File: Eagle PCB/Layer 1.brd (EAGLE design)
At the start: 196 x 185.3 mm, 247 parts, among them M1C1 33nF, M1C2 680uF, M1C3 1.0uF, M1D1 RED, M1D2 BLUE, M1J1 XT30PB-F, M1Q1 AOD482, M1R1 1k, M1R10 1k, M1R11 10k, M1R12 4.7k, M1R2 1k, M1R3 3.3k, M1R4 3.3k, M1R5 1k, M1R6 1k, M1R7 1k, M1R8 10k, M1R9 10k, M2C1 33nF, M2C2 680uF, M2C3 1.0uF, M2D1 RED, M2D2 BLUE, M2J1 XT30PB-F, M2Q1 AOD482, M2R1 1k, M2R10 1k, M2R11 10k, M2R12 4.7k, M2R2 1k, M2R3 3.3k, M2R4 3.3k, M2R5 1k, M2R6 1k, M2R7 1k, M2R8 10k, M2R9 10k, M3C1 33nF, M3C2 680uF, M3C3 1.0uF, M3D1 RED, M3D2 BLUE, M3J1 XT30PB-F, M3Q1 AOD482, M3R1 1k, M3R10 1k, M3R11 10k, M3R12 4.7k, M3R2 1k, M3R3 3.3k, M3R4 3.3k, M3R5 1k, M3R6 1k, M3R7 1k, M3R8 10k, M3R9 10k, M4C1 33nF, M4C2 680uF, M4C3 1.0uF, M4D1 RED, M4D2 BLUE, M4J1 XT30PB-F, M4Q1 AOD482, M4R1 1k, M4R10 1k, M4R11 10k, M4R12 4.7k, M4R2 1k, M4R3 3.3k, M4R4 3.3k, M4R5 1k, M4R6 1k, M4R7 1k, M4R8 10k, M4R9 10k, Q37 AO3402, X2 SM06B-SRSS-TB, Y1 8MHz

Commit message: Fucking Done
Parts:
- moved ESC_OUT 50.1 mm to (34.1, -75.6)
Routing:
- net V_BATT: track 292.6 -> 340.9 mm
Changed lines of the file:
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@@
 <attribute name="VALUE" x="-20.433" y="-71.66" size="0.7112" layer="27" font="vector" ratio="18" rot="R90" align="top-center"/>
 </element>
-<element name="ESC_OUT" library="JH" library_urn="urn:adsk.eagle:library:6027132" package="XT30PB-F" package3d_urn="urn:adsk.eagle:package:15925142/7" value="XT30PB-F" x="-15.84" y="-79.46" smashed="yes" rot="R270">
-<attribute name="NAME" x="-12.665" y="-74.38" size="1.27" layer="25" rot="R270"/>
+<element name="ESC_OUT" library="JH" library_urn="urn:adsk.eagle:library:6027132" package="XT30PB-F" package3d_urn="urn:adsk.eagle:package:15925142/7" value="XT30PB-F" x="34.06" y="-75.56" smashed="yes" rot="R270">
+<attribute name="NAME" x="37.235" y="-70.48" size="1.27" layer="25" rot="R270"/>
 </element>
 <element name="R8" library="JH" library_urn="urn:adsk.eagle:library:6027132" package="R0603" package3d_urn="urn:adsk.eagle:package:15441228/3" value="4.7k" x="-37.88" y="-77.18" smashed="yes" rot="R90">
@@
 <wire x1="-24.21" y1="-78.09" x2="-24.9" y2="-77.4" width="0.254" layer="1"/>
 <contactref element="ESC_OUT" pad="+"/>
-<wire x1="-15.84" y1="-76.96" x2="-19.14" y2="-76.96" width="0.508" layer="16"/>
-<wire x1="-19.14" y1="-76.96" x2="-24.2" y2="-71.9" width="0.508" layer="16"/>
+<wire x1="34.06" y1="-73.06" x2="-23.04" y2="-73.06" width="0.508" layer="16"/>
+<wire x1="-23.04" y1="-73.06" x2="-24.2" y2="-71.9" width="0.508" layer="16"/>
 <wire x1="25.857465625" y1="-17.3669375" x2="22.633059375" y2="14.14253125" width="0" layer="19" extent="1-1"/>
 <wire x1="-32.893753125" y1="32.263096875" x2="-1.061" y2="48.689" width="0" layer="19" extent="1-16"/>

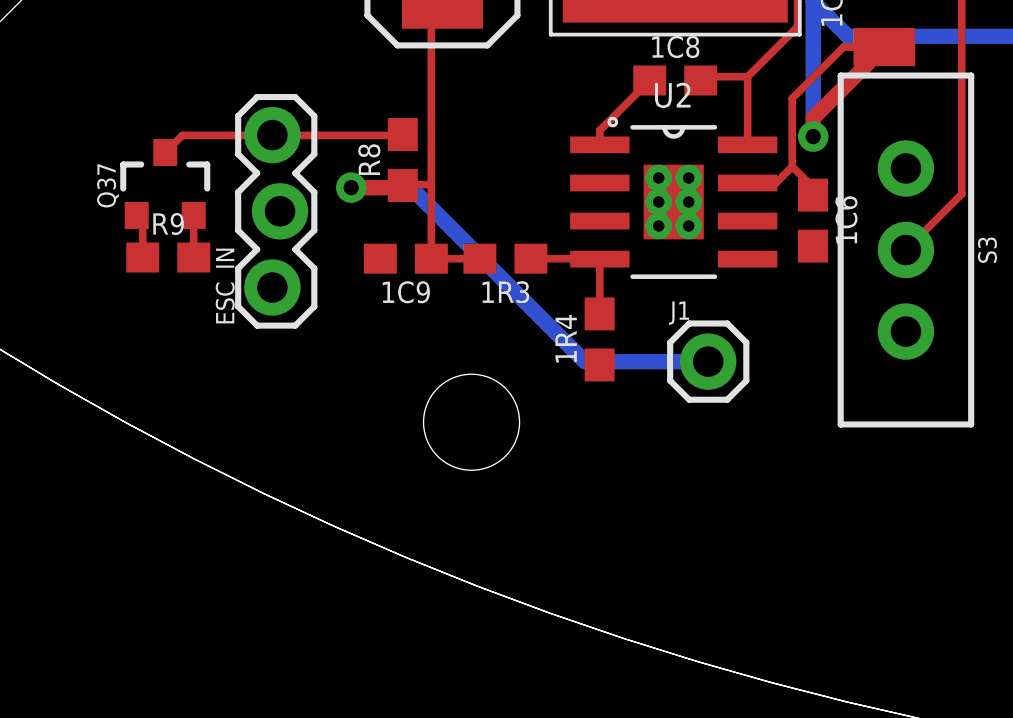
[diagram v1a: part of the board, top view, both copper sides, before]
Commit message: layer 1 esc fix
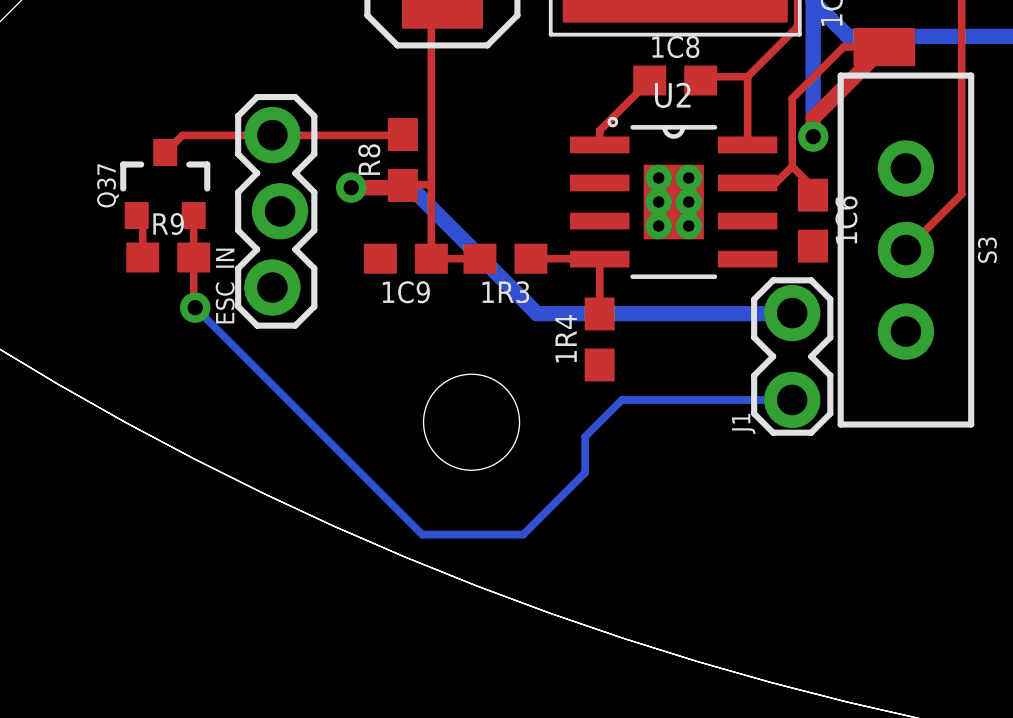
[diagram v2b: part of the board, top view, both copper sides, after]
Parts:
- J1: device Connectors:1X01 -> Connectors:1X02_LOCK
- moved J1 3.01 mm to (-24.9, -85.0), turned to 90 degrees
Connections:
- net 5V: now also J1.2; no longer J1.1
- net ESC_LV: now also J1.1
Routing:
- net ESC_LV: track 1.40 -> 28.7 mm, vias 0 -> 1
- net 5V: track 35.5 -> 37.6 mm
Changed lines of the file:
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@@
 </layers>
 <board>
-<fusionsync huburn="a.YnVzaW5lc3M6Z21haWwxNDMxNzc3" projecturn="a.YnVzaW5lc3M6Z21haWwxNDMxNzc3IzIwMjEwMTE1MzcxOTY3NzA2" f3durn="urn:adsk.wipprod:dm.lineage:Tavt4F5CTPSphMXKJUaMhw" pcbguid="" lastpulledtime="" lastsyncedchangeguid="" latestrevisionid="ff4a8119-30d6-4dfb-96ce-fc838807004c" lastsyncedrevisionid="ff4a8119-30d6-4dfb-96ce-fc838807004c" lastboardhashguid="9835a8ca-0695-94b5-924c-26b272f1dba1" lastpushedtime="2021-02-26T12:19:02Z" linktopcb3d="true"/>
+<fusionsync huburn="a.YnVzaW5lc3M6Z21haWwxNDMxNzc3" projecturn="a.YnVzaW5lc3M6Z21haWwxNDMxNzc3IzIwMjEwMTE1MzcxOTY3NzA2" f3durn="urn:adsk.wipprod:dm.lineage:Tavt4F5CTPSphMXKJUaMhw" pcbguid="" lastpulledtime="" lastsyncedchangeguid="" latestrevisionid="ff4a8119-30d6-4dfb-96ce-fc838807004c" lastsyncedrevisionid="ff4a8119-30d6-4dfb-96ce-fc838807004c" lastboardhashguid="9835a8ca-0695-94b5-924c-26b272f1dba1" lastpushedtime="2021-02-26T12:19:02Z" linktopcb3d="false"/>
 <plain>
 <circle x="88.919540625" y="-27.24548125" radius="1.6" width="0.001" layer="20"/>
@@
 <attribute name="VALUE" x="-40.068" y="-82.7" size="0.6096" layer="27" font="vector" ratio="20" rot="R90"/>
 </element>
-<element name="J1" library="Connectors" library_urn="urn:adsk.eagle:library:19813715" package="1X01" package3d_urn="urn:adsk.eagle:package:19813825/2" value="" x="-27.7" y="-83.9" smashed="yes">
-<attribute name="NAME" x="-28.97" y="-82.503" size="0.6096" layer="25" font="vector" ratio="20"/>
-<attribute name="VALUE" x="-28.97" y="-85.424" size="0.6096" layer="27" font="vector" ratio="20" align="top-left"/>
+<element name="J1" library="Connectors" library_urn="urn:adsk.eagle:library:19813715" package="1X02_LOCK" package3d_urn="urn:adsk.eagle:package:19813850/2" value="" x="-24.9" y="-85" smashed="yes" rot="R90">
+<attribute name="NAME" x="-26.297" y="-86.27" size="0.6096" layer="25" font="vector" ratio="20" rot="R90"/>
+<attribute name="VALUE" x="-22.868" y="-86.27" size="0.6096" layer="27" font="vector" ratio="20" rot="R90"/>
 </element>
 </elements>
@@
 <wire x1="-37.88" y1="-78.03" x2="-37.85" y2="-78" width="0.254" layer="1"/>
 <wire x1="-37.85" y1="-78" x2="-36.93" y2="-78" width="0.254" layer="1"/>
-<contactref element="J1" pad="1"/>
 <wire x1="-37.88" y1="-78.03" x2="-37.95" y2="-78.1" width="0.508" layer="1"/>
 <wire x1="-37.95" y1="-78.1" x2="-39.6" y2="-78.1" width="0.508" layer="1"/>
 <via x="-39.6" y="-78.1" extent="1-16" drill="0.508"/>
-<wire x1="-31.81" y1="-83.9" x2="-37.61" y2="-78.1" width="0.508" layer="16"/>
+<wire x1="-37.61" y1="-78.1" x2="-33.41" y2="-82.3" width="0.508" layer="16"/>
 <wire x1="-39.6" y1="-78.1" x2="-37.61" y2="-78.1" width="0.508" layer="16"/>
-<wire x1="-31.81" y1="-83.9" x2="-27.7" y2="-83.9" width="0.508" layer="16"/>
+<contactref element="J1" pad="2"/>
+<wire x1="-33.41" y1="-82.3" x2="-24.9178" y2="-82.3" width="0.508" layer="16"/>
+<wire x1="-24.9178" y1="-82.3" x2="-24.9" y2="-82.2822" width="0.508" layer="16"/>
 </signal>
 <signal name="ESC_HV">
@@
 <contactref element="Q37" pad="2"/>
 <wire x1="-44.85" y1="-80.43" x2="-44.85" y2="-79.03" width="0.254" layer="1"/>
+<contactref element="J1" pad="1"/>
+<wire x1="-44.85" y1="-80.43" x2="-44.85" y2="-82.05" width="0.254" layer="1"/>
+<wire x1="-44.85" y1="-82.05" x2="-44.8" y2="-82.1" width="0.254" layer="1"/>
+<via x="-44.8" y="-82.1" extent="1-16" drill="0.508"/>
+<wire x1="-44.8" y1="-82.1" x2="-37.2322" y2="-89.6678" width="0.254" layer="16"/>
+<wire x1="-33.87" y1="-89.6678" x2="-37.2322" y2="-89.6678" width="0.254" layer="16"/>
+<wire x1="-31.8011" y1="-87.5989" x2="-33.87" y2="-89.6678" width="0.254" layer="16"/>
+<wire x1="-31.8011" y1="-86.4011" x2="-31.8011" y2="-87.5989" width="0.254" layer="16"/>
+<wire x1="-24.9" y1="-85.1778" x2="-30.5778" y2="-85.1778" width="0.254" layer="16"/>
+<wire x1="-30.5778" y1="-85.1778" x2="-31.8011" y2="-86.4011" width="0.254" layer="16"/>
 </signal>
 <signal name="N$7">

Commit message: Revert "Layer 1 ESC fix"
This reverts commit 0f488ec0a57c37762cb3c7e9928ac58a828ee823.
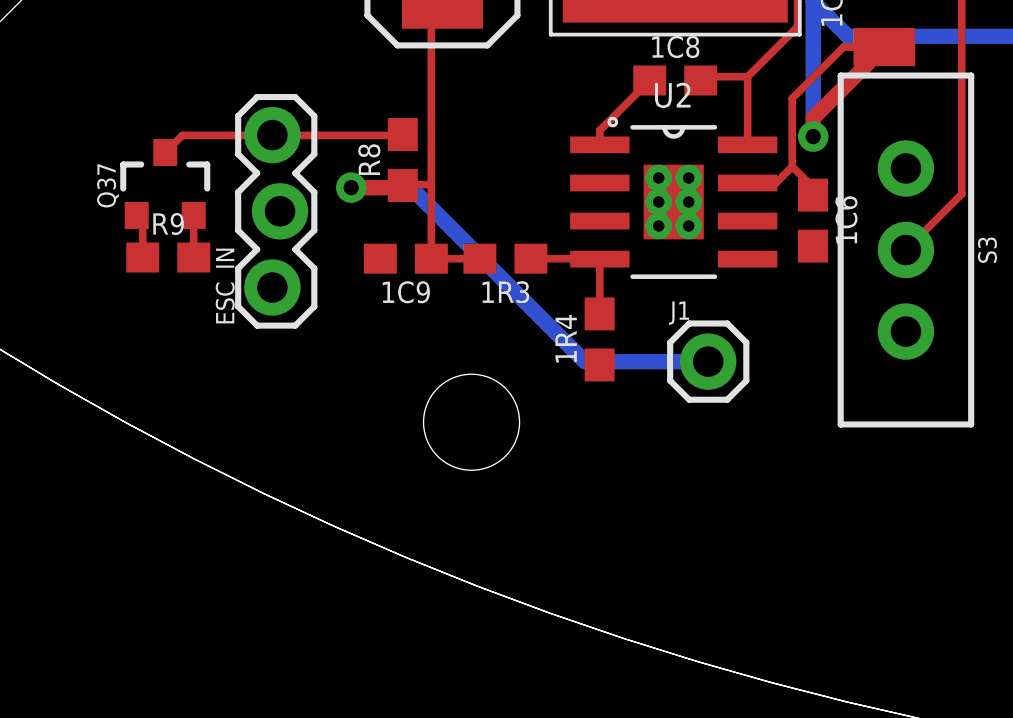
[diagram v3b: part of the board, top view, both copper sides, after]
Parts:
- J1: device Connectors:1X02_LOCK -> Connectors:1X01
- moved J1 3.01 mm to (-27.7, -83.9), turned to 0 degrees
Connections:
- net 5V: now also J1.1; no longer J1.2
- net ESC_LV: no longer J1.1
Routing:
- net ESC_LV: track 28.7 -> 1.40 mm, vias 1 -> 0
- net 5V: track 37.6 -> 35.5 mm
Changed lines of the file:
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@@
 </layers>
 <board>
-<fusionsync huburn="a.YnVzaW5lc3M6Z21haWwxNDMxNzc3" projecturn="a.YnVzaW5lc3M6Z21haWwxNDMxNzc3IzIwMjEwMTE1MzcxOTY3NzA2" f3durn="urn:adsk.wipprod:dm.lineage:Tavt4F5CTPSphMXKJUaMhw" pcbguid="" lastpulledtime="" lastsyncedchangeguid="" latestrevisionid="ff4a8119-30d6-4dfb-96ce-fc838807004c" lastsyncedrevisionid="ff4a8119-30d6-4dfb-96ce-fc838807004c" lastboardhashguid="9835a8ca-0695-94b5-924c-26b272f1dba1" lastpushedtime="2021-02-26T12:19:02Z" linktopcb3d="false"/>
+<fusionsync huburn="a.YnVzaW5lc3M6Z21haWwxNDMxNzc3" projecturn="a.YnVzaW5lc3M6Z21haWwxNDMxNzc3IzIwMjEwMTE1MzcxOTY3NzA2" f3durn="urn:adsk.wipprod:dm.lineage:Tavt4F5CTPSphMXKJUaMhw" pcbguid="" lastpulledtime="" lastsyncedchangeguid="" latestrevisionid="ff4a8119-30d6-4dfb-96ce-fc838807004c" lastsyncedrevisionid="ff4a8119-30d6-4dfb-96ce-fc838807004c" lastboardhashguid="9835a8ca-0695-94b5-924c-26b272f1dba1" lastpushedtime="2021-02-26T12:19:02Z" linktopcb3d="true"/>
 <plain>
 <circle x="88.919540625" y="-27.24548125" radius="1.6" width="0.001" layer="20"/>
@@
 <attribute name="VALUE" x="-40.068" y="-82.7" size="0.6096" layer="27" font="vector" ratio="20" rot="R90"/>
 </element>
-<element name="J1" library="Connectors" library_urn="urn:adsk.eagle:library:19813715" package="1X02_LOCK" package3d_urn="urn:adsk.eagle:package:19813850/2" value="" x="-24.9" y="-85" smashed="yes" rot="R90">
-<attribute name="NAME" x="-26.297" y="-86.27" size="0.6096" layer="25" font="vector" ratio="20" rot="R90"/>
-<attribute name="VALUE" x="-22.868" y="-86.27" size="0.6096" layer="27" font="vector" ratio="20" rot="R90"/>
+<element name="J1" library="Connectors" library_urn="urn:adsk.eagle:library:19813715" package="1X01" package3d_urn="urn:adsk.eagle:package:19813825/2" value="" x="-27.7" y="-83.9" smashed="yes">
+<attribute name="NAME" x="-28.97" y="-82.503" size="0.6096" layer="25" font="vector" ratio="20"/>
+<attribute name="VALUE" x="-28.97" y="-85.424" size="0.6096" layer="27" font="vector" ratio="20" align="top-left"/>
 </element>
 </elements>
@@
 <wire x1="-37.88" y1="-78.03" x2="-37.85" y2="-78" width="0.254" layer="1"/>
 <wire x1="-37.85" y1="-78" x2="-36.93" y2="-78" width="0.254" layer="1"/>
+<contactref element="J1" pad="1"/>
 <wire x1="-37.88" y1="-78.03" x2="-37.95" y2="-78.1" width="0.508" layer="1"/>
 <wire x1="-37.95" y1="-78.1" x2="-39.6" y2="-78.1" width="0.508" layer="1"/>
 <via x="-39.6" y="-78.1" extent="1-16" drill="0.508"/>
-<wire x1="-37.61" y1="-78.1" x2="-33.41" y2="-82.3" width="0.508" layer="16"/>
+<wire x1="-31.81" y1="-83.9" x2="-37.61" y2="-78.1" width="0.508" layer="16"/>
 <wire x1="-39.6" y1="-78.1" x2="-37.61" y2="-78.1" width="0.508" layer="16"/>
-<contactref element="J1" pad="2"/>
-<wire x1="-33.41" y1="-82.3" x2="-24.9178" y2="-82.3" width="0.508" layer="16"/>
-<wire x1="-24.9178" y1="-82.3" x2="-24.9" y2="-82.2822" width="0.508" layer="16"/>
+<wire x1="-31.81" y1="-83.9" x2="-27.7" y2="-83.9" width="0.508" layer="16"/>
 </signal>
 <signal name="ESC_HV">
@@
 <contactref element="Q37" pad="2"/>
 <wire x1="-44.85" y1="-80.43" x2="-44.85" y2="-79.03" width="0.254" layer="1"/>
-<contactref element="J1" pad="1"/>
-<wire x1="-44.85" y1="-80.43" x2="-44.85" y2="-82.05" width="0.254" layer="1"/>
-<wire x1="-44.85" y1="-82.05" x2="-44.8" y2="-82.1" width="0.254" layer="1"/>
-<via x="-44.8" y="-82.1" extent="1-16" drill="0.508"/>
-<wire x1="-44.8" y1="-82.1" x2="-37.2322" y2="-89.6678" width="0.254" layer="16"/>
-<wire x1="-33.87" y1="-89.6678" x2="-37.2322" y2="-89.6678" width="0.254" layer="16"/>
-<wire x1="-31.8011" y1="-87.5989" x2="-33.87" y2="-89.6678" width="0.254" layer="16"/>
-<wire x1="-31.8011" y1="-86.4011" x2="-31.8011" y2="-87.5989" width="0.254" layer="16"/>
-<wire x1="-24.9" y1="-85.1778" x2="-30.5778" y2="-85.1778" width="0.254" layer="16"/>
-<wire x1="-30.5778" y1="-85.1778" x2="-31.8011" y2="-86.4011" width="0.254" layer="16"/>
 </signal>
 <signal name="N$7">
